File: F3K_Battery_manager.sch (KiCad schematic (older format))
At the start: 13 parts, among them J1 Battery, J2 Coil, J3 Debug, J4 Serial, J5 Receiver, Q1 CSD13385F5, Q2 CSD13380F3, U1 DRV5032

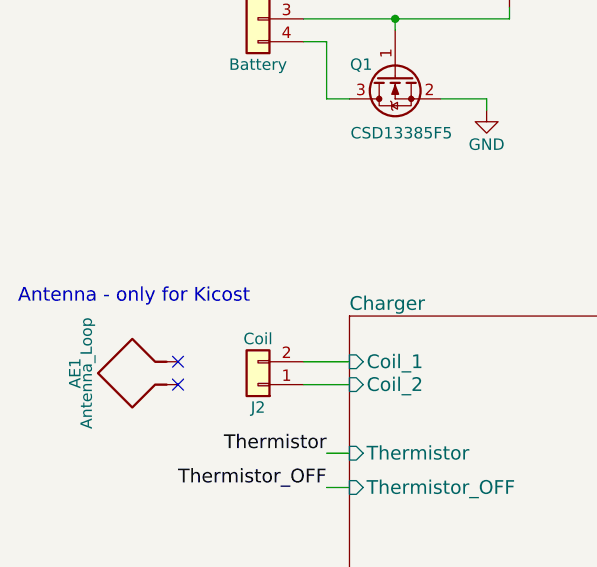
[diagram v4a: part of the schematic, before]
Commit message: Added resistor and capacitor values, footprints and NPNs
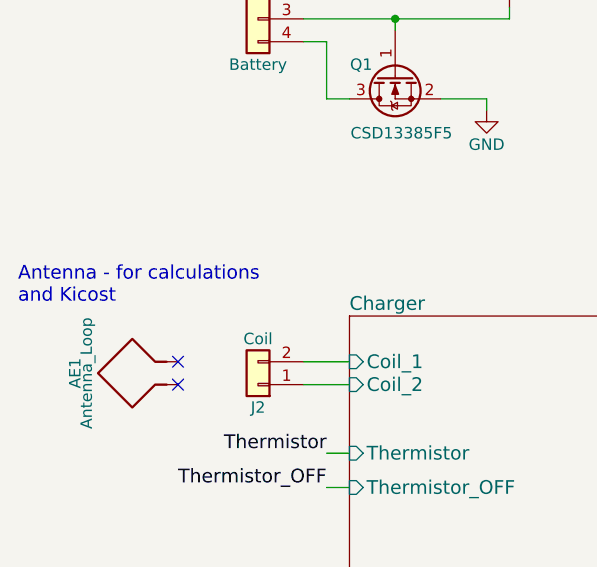
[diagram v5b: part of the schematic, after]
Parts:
- Q2: MPN (none) -> CSD13380F3
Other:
- note added: "Antenna - for calculations\nand Kicost\n"
- note removed: "Antenna - only for Kicost\n"
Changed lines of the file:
@@
 $EndComp
 $Comp
-L GND #PWR7
+L GND #PWR01
 U 1 1 5AA0735F
 P 4650 2500
-F 0 "#PWR7" H 4650 2250 50  0001 C CNN
+F 0 "#PWR01" H 4650 2250 50  0001 C CNN
 F 1 "GND" H 4650 2350 50  0000 C CNN
 F 2 "" H 4650 2500 50  0001 C CNN
@@
 $EndComp
 $Comp
-L GND #PWR8
+L GND #PWR02
 U 1 1 5AA07C91
 P 4650 3350
-F 0 "#PWR8" H 4650 3100 50  0001 C CNN
+F 0 "#PWR02" H 4650 3100 50  0001 C CNN
 F 1 "GND" H 4650 3200 50  0000 C CNN
 F 2 "" H 4650 3350 50  0001 C CNN
@@
 U 1 1 5AA08E27
 P 2850 5700
+AR Path="/5AA08E27" Ref="C1"  Part="1"
+AR Path="/5AA3AC9F/5AA08E27" Ref="C1"  Part="1"
 F 0 "C1" H 2875 5800 50  0000 L CNN
 F 1 "2u2 6V3" V 2700 5550 50  0000 L CNN
@@
 	4650 3300 4650 3350
 $Comp
-L GND #PWR6
+L GND #PWR03
 U 1 1 5AA09559
 P 3100 6000
-F 0 "#PWR6" H 3100 5750 50  0001 C CNN
+F 0 "#PWR03" H 3100 5750 50  0001 C CNN
 F 1 "GND" H 3100 5850 50  0000 C CNN
 F 2 "" H 3100 6000 50  0001 C CNN
@@
 Connection ~ 3100 5900
 $Comp
-L VDD #PWR5
+L VDD #PWR04
 U 1 1 5AA0982A
 P 3100 5400
-F 0 "#PWR5" H 3100 5250 50  0001 C CNN
+F 0 "#PWR04" H 3100 5250 50  0001 C CNN
 F 1 "VDD" H 3100 5550 50  0000 C CNN
 F 2 "" H 3100 5400 50  0001 C CNN
@@
 	3100 5500 3200 5500
 $Comp
-L VDD #PWR3
+L VDD #PWR05
 U 1 1 5AA09936
 P 2850 5400
-F 0 "#PWR3" H 2850 5250 50  0001 C CNN
+F 0 "#PWR05" H 2850 5250 50  0001 C CNN
 F 1 "VDD" H 2850 5550 50  0000 C CNN
 F 2 "" H 2850 5400 50  0001 C CNN
@@
 $EndComp
 $Comp
-L GND #PWR4
+L GND #PWR06
 U 1 1 5AA0996B
 P 2850 6000
-F 0 "#PWR4" H 2850 5750 50  0001 C CNN
+F 0 "#PWR06" H 2850 5750 50  0001 C CNN
 F 1 "GND" H 2850 5850 50  0000 C CNN
 F 2 "" H 2850 6000 50  0001 C CNN
@@
 	7200 2450 7200 2500
 $Comp
-L GND #PWR10
+L GND #PWR07
 U 1 1 5AA112B0
 P 7200 3150
-F 0 "#PWR10" H 7200 2900 50  0001 C CNN
+F 0 "#PWR07" H 7200 2900 50  0001 C CNN
 F 1 "GND" H 7200 3000 50  0000 C CNN
 F 2 "" H 7200 3150 50  0001 C CNN
@@
 	6600 2700 6900 2700
 $Comp
-L +BATT #PWR9
+L +BATT #PWR08
 U 1 1 5AA3F1DA
 P 7200 2150
-F 0 "#PWR9" H 7200 2000 50  0001 C CNN
+F 0 "#PWR08" H 7200 2000 50  0001 C CNN
 F 1 "+BATT" H 7200 2290 50  0000 C CNN
 F 2 "" H 7200 2150 50  0001 C CNN
@@
 	9150 4000 10100 4000
 $Comp
-L GND #PWR11
+L GND #PWR09
 U 1 1 5AA460B2
 P 9300 4300
-F 0 "#PWR11" H 9300 4050 50  0001 C CNN
+F 0 "#PWR09" H 9300 4050 50  0001 C CNN
 F 1 "GND" H 9300 4150 50  0000 C CNN
 F 2 "" H 9300 4300 50  0001 C CNN
@@
 	2300 2550 2300 2550
 $Comp
-L +BATT #PWR2
+L +BATT #PWR010
 U 1 1 5AA74E47
 P 2800 2500
-F 0 "#PWR2" H 2800 2350 50  0001 C CNN
+F 0 "#PWR010" H 2800 2350 50  0001 C CNN
 F 1 "+BATT" H 2800 2640 50  0000 C CNN
 F 2 "" H 2800 2500 50  0001 C CNN
@@
 Connection ~ 2300 2550
 $Comp
-L GND #PWR1
+L GND #PWR011
 U 1 1 5AA7526D
 P 2700 2950
-F 0 "#PWR1" H 2700 2700 50  0001 C CNN
+F 0 "#PWR011" H 2700 2700 50  0001 C CNN
 F 1 "GND" H 2700 2800 50  0000 C CNN
 F 2 "" H 2700 2950 50  0001 C CNN
@@
 NoConn ~ 1350 4150
 Text Notes 650  3800 0    60   ~ 0
-Antenna - only for Kicost\n
+Antenna - for calculations\nand Kicost\n
 Wire Wire Line
 	4250 4550 4850 4550
@@
 F 2 "" H 7300 2625 50  0001 L CIN
 F 3 "http://www.ti.com/product/CSD13380F3" H 6400 2400 50  0001 L CNN
+F 4 "CSD13380F3" H 7100 2700 60  0001 C CNN "MPN"
 	1    7100 2700
 	1    0    0    -1

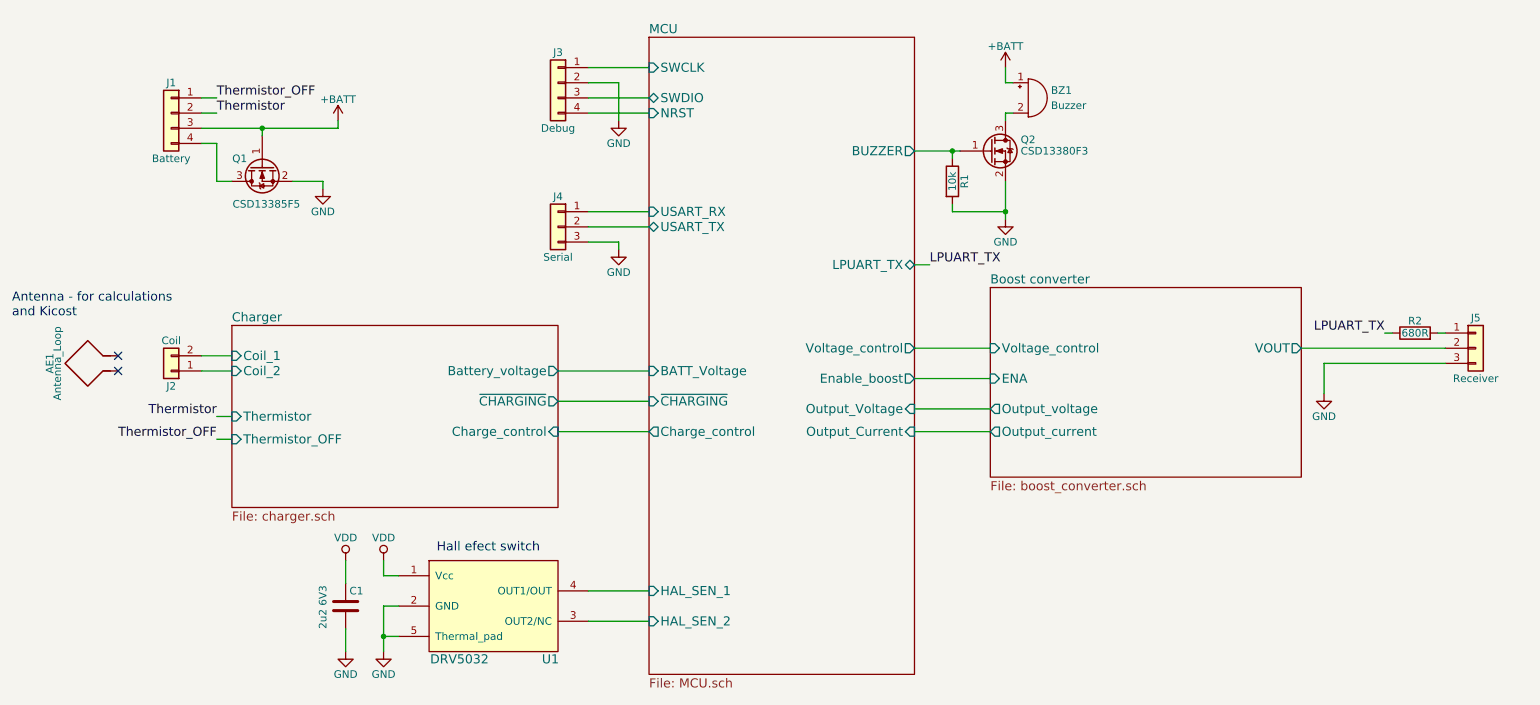
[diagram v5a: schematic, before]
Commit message: Removed boost converter, added output switch
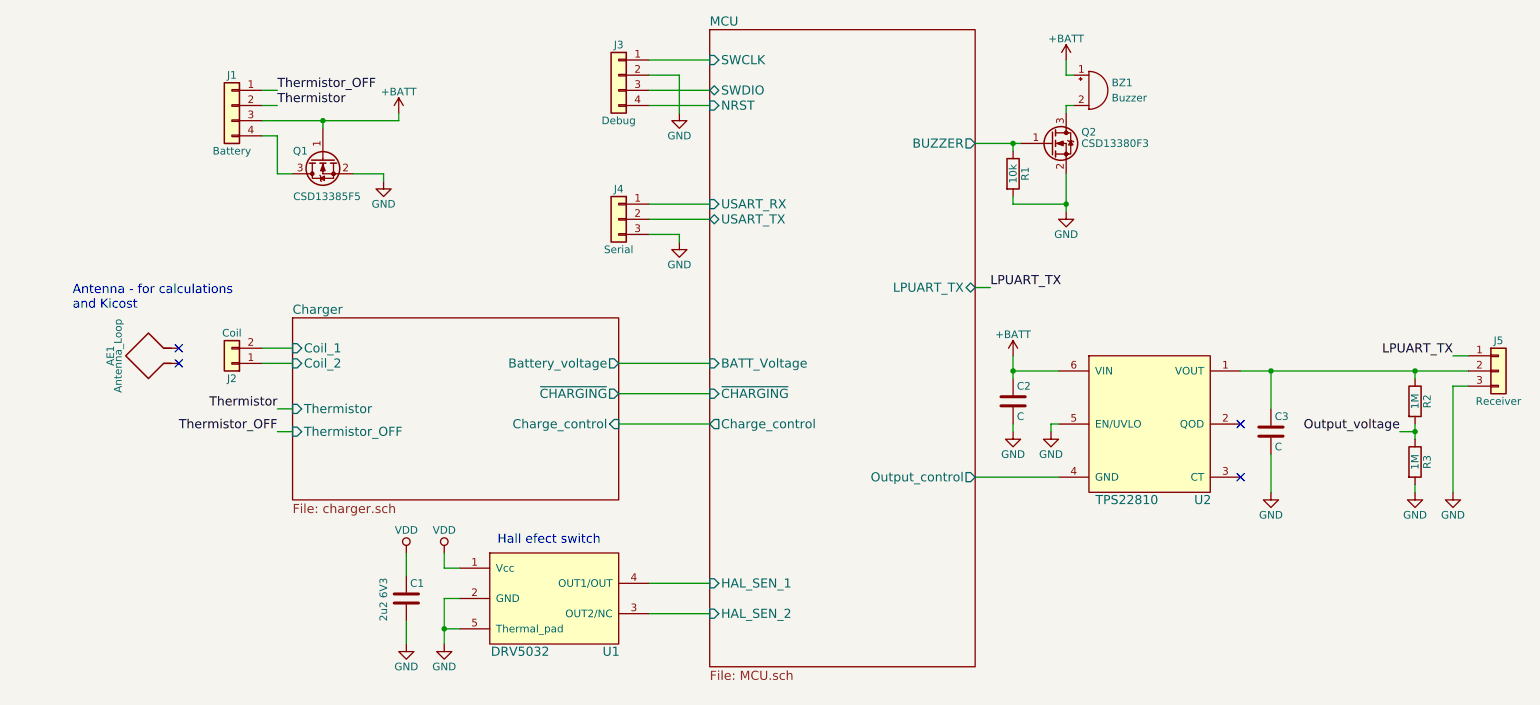
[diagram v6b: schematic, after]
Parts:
- added C2, C3: C, symbol C
- added R3: 1M, Resistors_SMD:R_0402, symbol R
- added U2: TPS22810, lakotamm-miscellaneous:WSON-6_2x2mm_Pitch0.65mm, symbol TPS22810
- R2: value 680R -> 1M
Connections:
- net +BATT: now also C2.1, U2.6 (VIN)
- net GND: now also C2.2, C3.2, R3.2, U2.5 (EN/UVLO)
- net LPUART_TX: now also J5.1 (Pin_1); no longer R2.1
- net Output_voltage: now reaches R2.2
- net Output_voltage: now also R3.1; no longer J5.1 (Pin_1)
- net Boost converter/VOUT: no longer names the net of J5.2 (Pin_2)
- net Boost converter/VOUT: now also R2.1, C3.1, U2.1 (VOUT)
- new net MCU/Output_control: U2.4 (GND)
- no-connect marks 2 -> 4
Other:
- moved on the sheet: AE1, BZ1, C1, J1, J2, J3, J4, J5, Q1, Q2, R1, U1

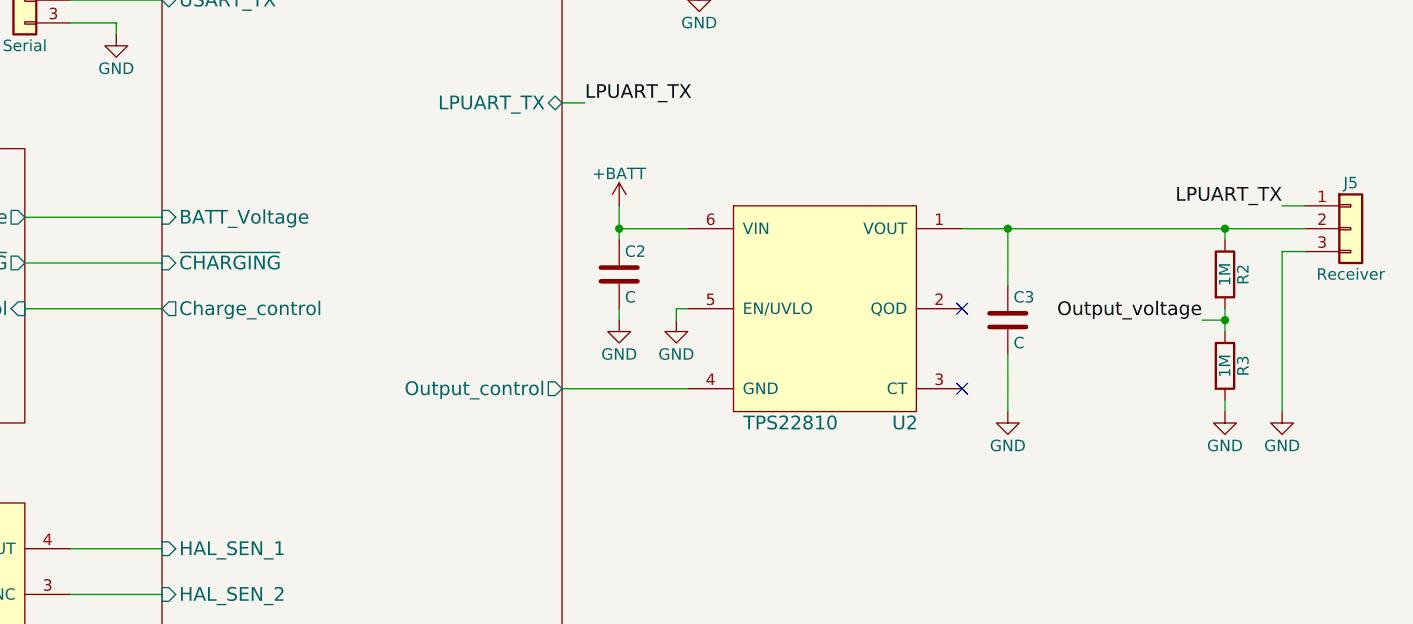
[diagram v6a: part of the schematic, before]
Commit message: Added output stage sheet
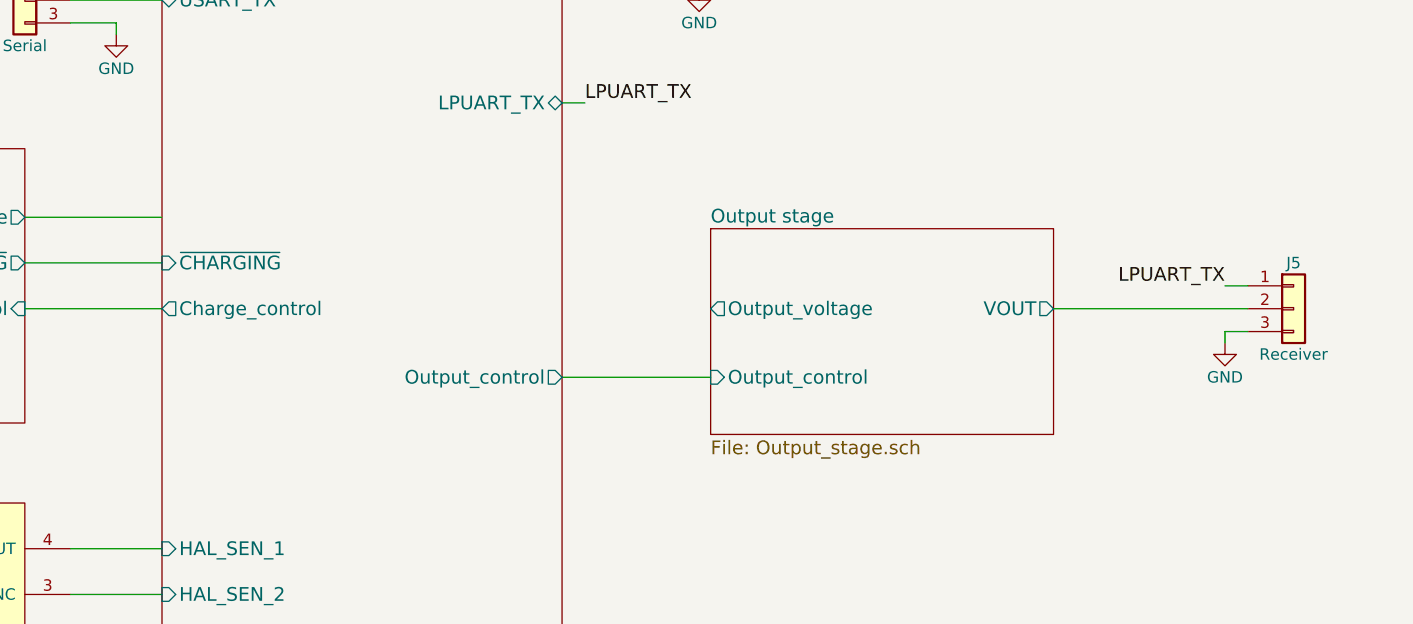
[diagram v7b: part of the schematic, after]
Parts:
- removed C2, C3: C, symbol C
- removed R2, R3: 1M, Resistors_SMD:R_0402, symbol R
- removed U2: TPS22810, lakotamm-miscellaneous:WSON-6_2x2mm_Pitch0.65mm, symbol TPS22810
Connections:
- net Output stage/VOUT: now reaches J5.2 (Pin_2)
- no-connect marks 4 -> 2
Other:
- moved on the sheet: J5
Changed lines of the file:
@@
 $Descr A4 11693 8268
 encoding utf-8
-Sheet 1 3
+Sheet 1 4
 Title ""
 Date ""
@@
 Comment4 ""
 $EndDescr
-$Sheet
-S 5250 1900 1750 4200
-U 5A9B3060
-F0 "MCU" 60
-F1 "MCU.sch" 60
-F2 "NRST" I L 5250 2400 60
-F3 "SWCLK" I L 5250 2100 60
-F4 "SWDIO" B L 5250 2300 60
-F5 "USART_RX" I L 5250 3050 60
-F6 "HAL_SEN_1" I L 5250 5550 60
-F7 "HAL_SEN_2" I L 5250 5750 60
-F8 "BUZZER" O R 7000 2650 60
-F9 "BATT_Voltage" I L 5250 4100 60
-F10 "USART_TX" B L 5250 3150 60
-F11 "~CHARGING" I L 5250 4300 60
-F12 "Charge_control" O L 5250 4500 60
-F13 "LPUART_TX" B R 7000 3600 60
-F14 "Output_control" O R 7000 4850 60
-$EndSheet
 $Comp
 L Conn_01x04 J3
@@
 L Conn_01x03 J5
 U 1 1 5AA45C5D
-P 10450 4150
-F 0 "J5" H 10450 4350 50  0000 C CNN
-F 1 "Receiver" H 10450 3950 50  0000 C CNN
-F 2 "" H 10450 4150 50  0001 C CNN
-F 3 "" H 10450 4150 50  0001 C CNN
-	1    10450 4150
+P 10200 4500
+F 0 "J5" H 10200 4700 50  0000 C CNN
+F 1 "Receiver" H 10200 4300 50  0000 C CNN
+F 2 "" H 10200 4500 50  0001 C CNN
+F 3 "" H 10200 4500 50  0001 C CNN
+	1    10200 4500
 	1    0    0    -1
 $EndComp
@@
 $EndComp
 $Comp
-L C C2
-U 1 1 5ABF6D8D
-P 7250 4350
-F 0 "C2" H 7275 4450 50  0000 L CNN
-F 1 "C" H 7275 4250 50  0000 L CNN
-F 2 "" H 7288 4200 50  0001 C CNN
-F 3 "" H 7250 4350 50  0001 C CNN
-	1    7250 4350
-	1    0    0    -1
-$EndComp
-$Comp
-L TPS22810 U2
-U 1 1 5ABFFB1E
-P 8150 4500
-F 0 "U2" H 8500 4000 60  0000 C CNN
-F 1 "TPS22810" H 8000 4000 60  0000 C CNN
-F 2 "lakotamm-miscellaneous:WSON-6_2x2mm_Pitch0.65mm" H 8150 3450 60  0001 C CNN
-F 3 "http://www.ti.com/lit/ds/symlink/tps22810.pdf" H 8150 3650 60  0001 C CNN
-F 4 "TPS22810DRV" H 8200 3550 60  0001 C CNN "MPN"
-	1    8150 4500
-	1    0    0    -1
-$EndComp
-NoConn ~ 8750 4500
-$Comp
-L +BATT #PWR9
-U 1 1 5AC00847
-P 7250 4050
-F 0 "#PWR9" H 7250 3900 50  0001 C CNN
-F 1 "+BATT" H 7250 4190 50  0000 C CNN
-F 2 "" H 7250 4050 50  0001 C CNN
-F 3 "" H 7250 4050 50  0001 C CNN
-	1    7250 4050
-	1    0    0    -1
-$EndComp
-$Comp
-L GND #PWR10
-U 1 1 5AC015AF
-P 7250 4550
-F 0 "#PWR10" H 7250 4300 50  0001 C CNN
-F 1 "GND" H 7250 4400 50  0000 C CNN
-F 2 "" H 7250 4550 50  0001 C CNN
-F 3 "" H 7250 4550 50  0001 C CNN
-	1    7250 4550
-	1    0    0    -1
-$EndComp
-$Comp
 L GND #PWR16
 U 1 1 5AC01FB1
-P 10150 4950
-F 0 "#PWR16" H 10150 4700 50  0001 C CNN
-F 1 "GND" H 10150 4800 50  0000 C CNN
-F 2 "" H 10150 4950 50  0001 C CNN
-F 3 "" H 10150 4950 50  0001 C CNN
-	1    10150 4950
-	1    0    0    -1
-$EndComp
-Text Label 10150 4050 2    60   ~ 0
+P 9900 4650
+F 0 "#PWR16" H 9900 4400 50  0001 C CNN
+F 1 "GND" H 9900 4500 50  0000 C CNN
+F 2 "" H 9900 4650 50  0001 C CNN
+F 3 "" H 9900 4650 50  0001 C CNN
+	1    9900 4650
+	1    0    0    -1
+$EndComp
+Text Label 9900 4400 2    60   ~ 0
 LPUART_TX
-$Comp
-L GND #PWR11
-U 1 1 5AC0318E
-P 7500 4550
-F 0 "#PWR11" H 7500 4300 50  0001 C CNN
-F 1 "GND" H 7500 4400 50  0000 C CNN
-F 2 "" H 7500 4550 50  0001 C CNN
-F 3 "" H 7500 4550 50  0001 C CNN
-	1    7500 4550
-	1    0    0    -1
-$EndComp
-NoConn ~ 8750 4850
-$Comp
-L C C3
-U 1 1 5AC077A4
-P 8950 4550
-F 0 "C3" H 8975 4650 50  0000 L CNN
-F 1 "C" H 8975 4450 50  0000 L CNN
-F 2 "" H 8988 4400 50  0001 C CNN
-F 3 "" H 8950 4550 50  0001 C CNN
-	1    8950 4550
-	1    0    0    -1
-$EndComp
-$Comp
-L GND #PWR14
-U 1 1 5AC077AA
-P 8950 4950
-F 0 "#PWR14" H 8950 4700 50  0001 C CNN
-F 1 "GND" H 8950 4800 50  0000 C CNN
-F 2 "" H 8950 4950 50  0001 C CNN
-F 3 "" H 8950 4950 50  0001 C CNN
-	1    8950 4950
-	1    0    0    -1
-$EndComp
-$Comp
-L R R2
-U 1 1 5AC0CC9F
-P 9900 4350
-F 0 "R2" V 9980 4350 50  0000 C CNN
-F 1 "1M" V 9900 4350 50  0000 C CNN
-F 2 "Resistors_SMD:R_0402" V 9830 4350 50  0001 C CNN
-F 3 "" H 9900 4350 50  0001 C CNN
-	1    9900 4350
-	1    0    0    -1
-$EndComp
-$Comp
-L R R3
-U 1 1 5AC0CDB1
-P 9900 4750
-F 0 "R3" V 9980 4750 50  0000 C CNN
-F 1 "1M" V 9900 4750 50  0000 C CNN
-F 2 "Resistors_SMD:R_0402" V 9830 4750 50  0001 C CNN
-F 3 "" H 9900 4750 50  0001 C CNN
-	1    9900 4750
-	1    0    0    -1
-$EndComp
-$Comp
-L GND #PWR15
-U 1 1 5AC0DFF1
-P 9900 4950
-F 0 "#PWR15" H 9900 4700 50  0001 C CNN
-F 1 "GND" H 9900 4800 50  0000 C CNN
-F 2 "" H 9900 4950 50  0001 C CNN
-F 3 "" H 9900 4950 50  0001 C CNN
-	1    9900 4950
-	1    0    0    -1
-$EndComp
 Wire Wire Line
 	4850 2100 5250 2100
@@
 	7100 3600 7000 3600
 Wire Wire Line
-	7250 4050 7250 4200
-Wire Wire Line
-	7250 4150 7550 4150
-Connection ~ 7250 4150
-Wire Wire Line
-	8750 4150 10250 4150
-Wire Wire Line
-	10250 4250 10150 4250
-Wire Wire Line
-	10150 4250 10150 4950
-Wire Wire Line
-	10250 4050 10150 4050
-Wire Wire Line
-	7250 4500 7250 4550
-Wire Wire Line
-	7550 4500 7500 4500
-Wire Wire Line
-	7500 4500 7500 4550
-Wire Wire Line
-	8950 4700 8950 4950
-Wire Wire Line
-	7000 4850 7550 4850
-Wire Wire Line
-	9900 4200 9900 4150
-Connection ~ 9900 4150
-Wire Wire Line
-	9900 4500 9900 4600
-Wire Wire Line
-	9900 4900 9900 4950
-Wire Wire Line
-	8950 4400 8950 4150
-Connection ~ 8950 4150
-Text Label 9800 4550 2    60   ~ 0
-Output_voltage
-Wire Wire Line
-	9800 4550 9900 4550
-Connection ~ 9900 4550
+	10000 4600 9900 4600
+Wire Wire Line
+	9900 4600 9900 4650
+Wire Wire Line
+	10000 4400 9900 4400
+$Sheet
+S 5250 1900 1750 4200
+U 5A9B3060
+F0 "MCU" 60
+F1 "MCU.sch" 60
+F2 "NRST" I L 5250 2400 60
+F3 "SWCLK" I L 5250 2100 60
+F4 "SWDIO" B L 5250 2300 60
+F5 "USART_RX" I L 5250 3050 60
+F6 "HAL_SEN_1" I L 5250 5550 60
+F7 "HAL_SEN_2" I L 5250 5750 60
+F8 "BUZZER" O R 7000 2650 60
+F9 "USART_TX" B L 5250 3150 60
+F10 "~CHARGING" I L 5250 4300 60
+F11 "Charge_control" O L 5250 4500 60
+F12 "LPUART_TX" B R 7000 3600 60
+F13 "Output_control" O R 7000 4800 60
+$EndSheet
+$Sheet
+S 7650 4150 1500 900
+U 5AC06660
+F0 "Output stage" 60
+F1 "Output_stage.sch" 60
+F2 "Output_control" I L 7650 4800 60
+F3 "Output_voltage" O L 7650 4500 60
+F4 "VOUT" O R 9150 4500 60
+$EndSheet
+Wire Wire Line
+	9150 4500 10000 4500
+Wire Wire Line
+	7650 4800 7000 4800
 $EndSCHEMATC
